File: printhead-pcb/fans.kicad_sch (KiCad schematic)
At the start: 18 parts, among them J1 FAN0, J2 FAN2, J3 FAN1, J4 FAN3, Q1 DTC143E, Q2 DTC143E, Q3 DTC143E, Q4 DTC143E, U1 EMC2302-1-AIZL-TR, U2 EMC2302-2-AIZL-TR

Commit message: layout
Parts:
- removed U1: EMC2302-1-AIZL-TR, EMC2302-1-AIZL-TR:MSOP10_MC_MCH-M, symbol EMC2302-1-AIZL-TR:EMC2302-1-AIZL-TR
- added U1: EMC2302-2-AIZL-TR, EMC2302-2-AIZL-TR:MSOP10_MC_MCH, symbol EMC2302-2-AIZL-TR:EMC2302-2-AIZL-TR
- J2: renamed from J1; footprint Connector_JST:JST_GH_SM02B-GHS-TB_1x02-1MP_P1.25mm_Horizontal -> Connector_JST:JST_EH_S2B-EH_1x02_P2.50mm_Horizontal
- J3: renamed from J2; footprint Connector_JST:JST_GH_SM02B-GHS-TB_1x02-1MP_P1.25mm_Horizontal -> Connector_JST:JST_EH_B2B-EH-A_1x02_P2.50mm_Vertical
- J4: renamed from J3; footprint Connector_JST:JST_GH_SM02B-GHS-TB_1x02-1MP_P1.25mm_Horizontal -> Connector_JST:JST_EH_S2B-EH_1x02_P2.50mm_Horizontal
- J5: renamed from J4; footprint Connector_JST:JST_GH_SM02B-GHS-TB_1x02-1MP_P1.25mm_Horizontal -> Connector_JST:JST_EH_B2B-EH-A_1x02_P2.50mm_Vertical
- R6: renamed from R5; value 3k3 -> 10k
- R7: renamed from R6; value 3k3 -> 10k
- U2: footprint EMC2302-1-AIZL-TR:MSOP10_MC_MCH-M -> EMC2302-2-AIZL-TR:MSOP10_MC_MCH
- renumbered R9 to R10, R10 to R11, R3 to R4, R4 to R5, R7 to R8, R8 to R9
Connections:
- net +3V3: now also U1.3 (VDD)
- net FAN_0_PWM: now also U1.5 (PWM1)
- net FAN_1_PWM: now also U1.7 (PWM2)
- net GND: now also U1.4 (GND)
- net SCL: now also U1.2 (SMCLK)
- net SDA: now also U1.1 (SMDATA)
- net at R6.1: now also U1.10 (*ALERT)
- net at R4.1: now also U1.6 (TACH1)
- net at R8.1: now also U1.8 (TACH2)
- net at R10.1: now also U1.9 (CLK)

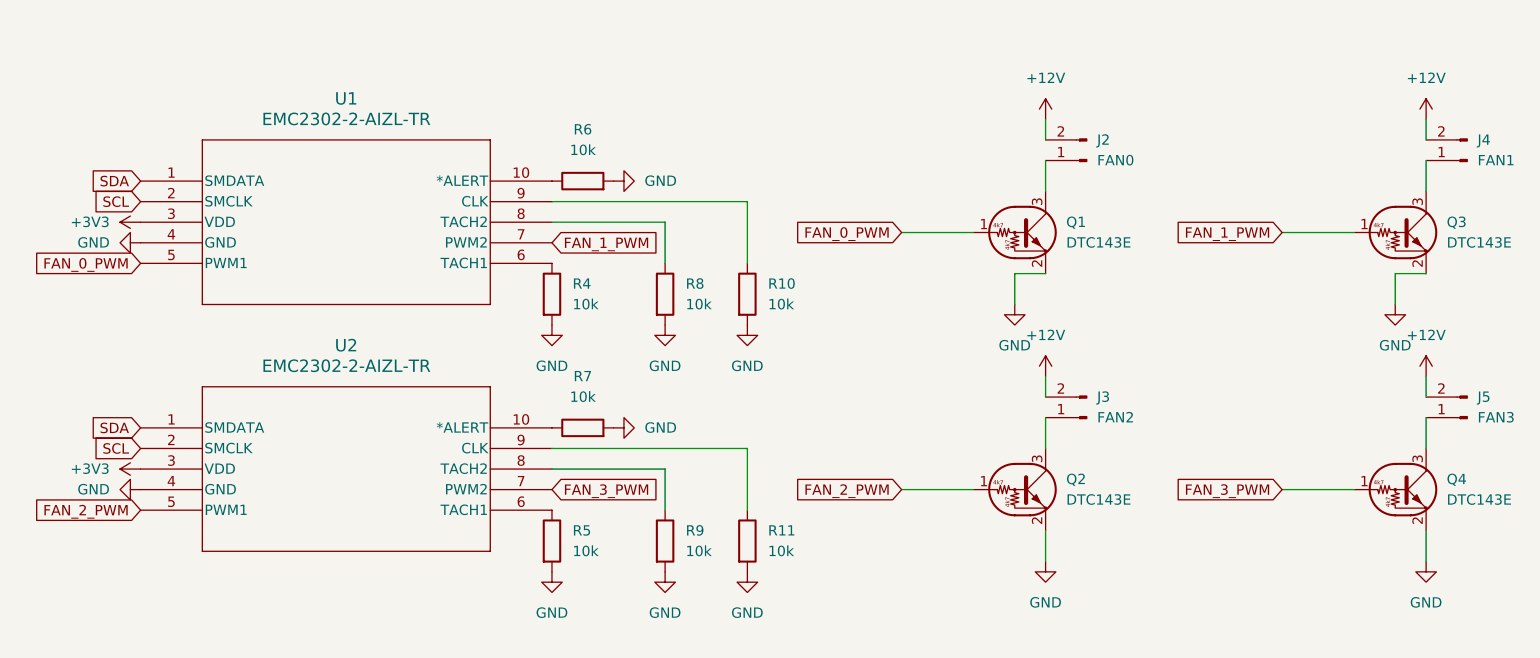
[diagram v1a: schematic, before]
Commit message: add pwr, gnd 5V for di2c chip
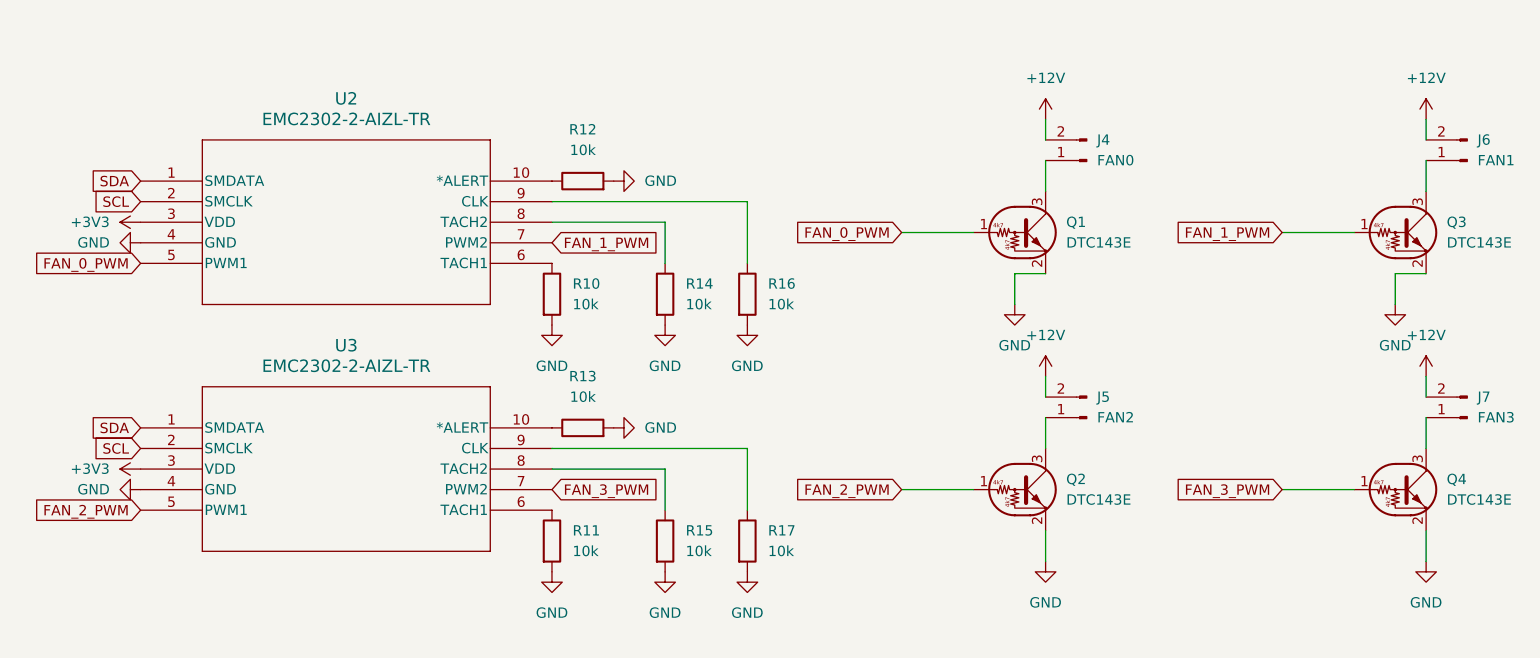
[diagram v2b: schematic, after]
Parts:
- renumbered J2 to J4, J3 to J5, J4 to J6, J5 to J7, R4 to R10, R5 to R11, R6 to R12, R7 to R13, R8 to R14, R9 to R15, R10 to R16, R11 to R17, U1 to U2, U2 to U3

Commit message: added voltage converter
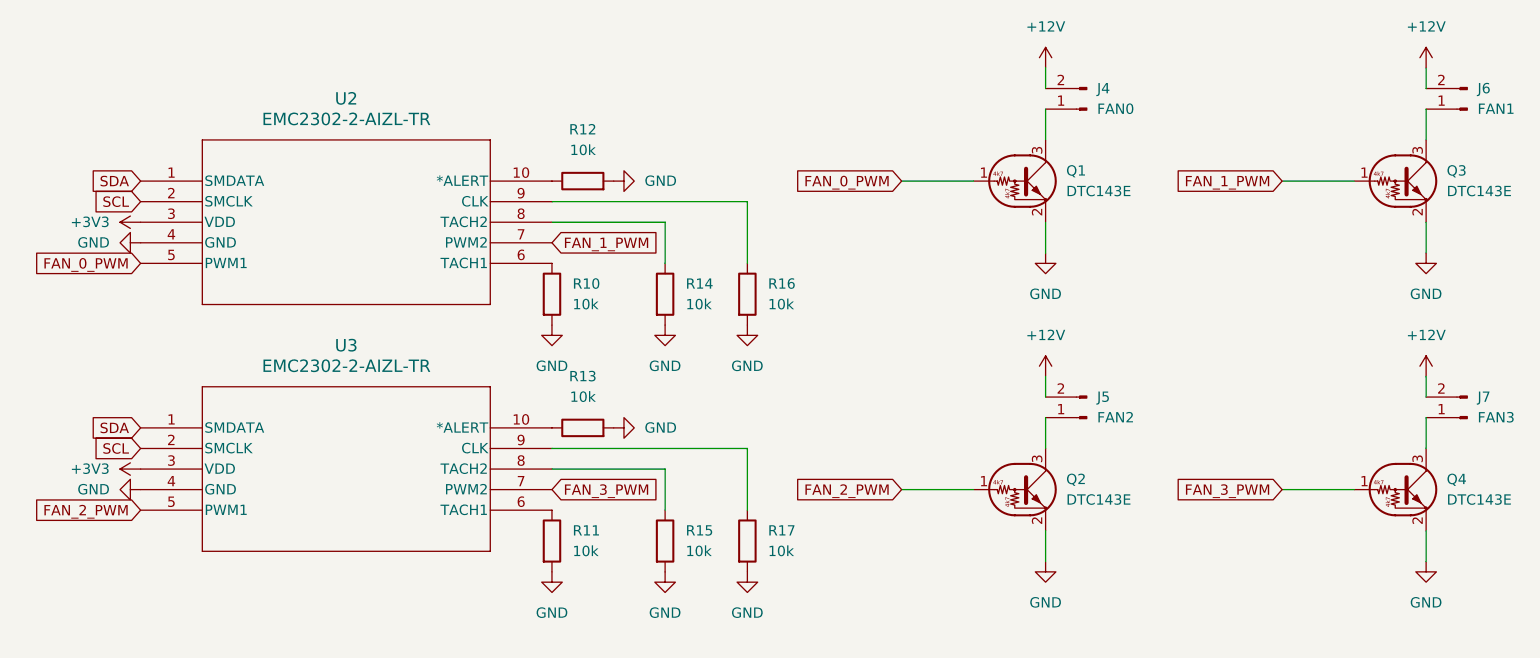
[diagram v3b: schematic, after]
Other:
- moved on the sheet: J4, J6, Q1, Q3
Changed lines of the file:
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@@
 	(wire
 		(pts
-			(xy 162.56 83.82) (xy 171.45 83.82)
+			(xy 162.56 77.47) (xy 171.45 77.47)
 		)
 		(stroke
@@
 	(wire
 		(pts
-			(xy 180.34 69.85) (xy 180.34 72.39)
+			(xy 180.34 63.5) (xy 180.34 66.04)
 		)
 		(stroke
@@
 	(wire
 		(pts
-			(xy 180.34 74.93) (xy 180.34 78.74)
+			(xy 180.34 68.58) (xy 180.34 72.39)
 		)
 		(stroke
@@
 	(wire
 		(pts
-			(xy 227.33 69.85) (xy 227.33 72.39)
+			(xy 227.33 63.5) (xy 227.33 66.04)
 		)
 		(stroke
@@
 	(wire
 		(pts
-			(xy 223.52 88.9) (xy 227.33 88.9)
+			(xy 180.34 106.68) (xy 180.34 110.49)
 		)
 		(stroke
@@
 	(wire
 		(pts
-			(xy 180.34 106.68) (xy 180.34 110.49)
+			(xy 133.35 82.55) (xy 119.38 82.55)
 		)
 		(stroke
@@
 	(wire
 		(pts
-			(xy 133.35 82.55) (xy 119.38 82.55)
+			(xy 227.33 68.58) (xy 227.33 72.39)
 		)
 		(stroke
@@
 	(wire
 		(pts
-			(xy 227.33 74.93) (xy 227.33 78.74)
+			(xy 180.34 82.55) (xy 180.34 86.36)
 		)
 		(stroke
@@
 	(wire
 		(pts
-			(xy 176.53 88.9) (xy 176.53 92.71)
+			(xy 209.55 77.47) (xy 218.44 77.47)
 		)
 		(stroke
@@
 	(wire
 		(pts
-			(xy 209.55 83.82) (xy 218.44 83.82)
+			(xy 180.34 101.6) (xy 180.34 104.14)
 		)
 		(stroke
@@
 	(wire
 		(pts
-			(xy 180.34 101.6) (xy 180.34 104.14)
+			(xy 227.33 82.55) (xy 227.33 86.36)
 		)
 		(stroke
@@
 	(wire
 		(pts
-			(xy 223.52 88.9) (xy 223.52 92.71)
+			(xy 227.33 101.6) (xy 227.33 104.14)
 		)
 		(stroke
@@
 		)
 	)
-	(wire
-		(pts
-			(xy 176.53 88.9) (xy 180.34 88.9)
-		)
-		(stroke
-			(width 0)
-			(type default)
-		)
-	)
-	(wire
-		(pts
-			(xy 227.33 101.6) (xy 227.33 104.14)
-		)
-		(stroke
-			(width 0)
-			(type default)
-		)
-	)
 	(global_label "FAN_3_PWM"
 		(shape input)
@@
 	(global_label "FAN_0_PWM"
 		(shape input)
-		(at 162.56 83.82 180)
+		(at 162.56 77.47 180)
 		(fields_autoplaced yes)
 		(effects
@@
 		)
 		(property "Intersheetrefs" "${INTERSHEET_REFS}"
-			(at 148.7496 83.82 0)
+			(at 148.7496 77.47 0)
 			(effects
 				(font
@@
 	(global_label "FAN_1_PWM"
 		(shape input)
-		(at 209.55 83.82 180)
+		(at 209.55 77.47 180)
 		(fields_autoplaced yes)
 		(effects
@@
 		)
 		(property "Intersheetrefs" "${INTERSHEET_REFS}"
-			(at 195.7396 83.82 0)
+			(at 195.7396 77.47 0)
 			(effects
 				(font
@@
 	(symbol
 		(lib_id "power:+12V")
-		(at 180.34 69.85 0)
+		(at 180.34 63.5 0)
 		(unit 1)
 		(exclude_from_sim no)
@@
 		(fields_autoplaced yes)
 		(property "Reference" "#PWR032"
-			(at 180.34 73.66 0)
+			(at 180.34 67.31 0)
 			(effects
 				(font
@@
 		)
 		(property "Value" "+12V"
-			(at 180.34 64.77 0)
+			(at 180.34 58.42 0)
 			(effects
 				(font
@@
 		)
 		(property "Footprint" ""
-			(at 180.34 69.85 0)
+			(at 180.34 63.5 0)
 			(effects
 				(font
@@
 		)
 		(property "Datasheet" ""
-			(at 180.34 69.85 0)
+			(at 180.34 63.5 0)
 			(effects
 				(font
@@
 		)
 		(property "Description" "Power symbol creates a global label with name \"+12V\""
-			(at 180.34 69.85 0)
+			(at 180.34 63.5 0)
 			(effects
 				(font
@@
 	(symbol
 		(lib_id "power:GND")
-		(at 176.53 92.71 0)
+		(at 180.34 86.36 0)
 		(unit 1)
 		(exclude_from_sim no)
@@
 		(fields_autoplaced yes)
 		(property "Reference" "#PWR031"
-			(at 176.53 99.06 0)
+			(at 180.34 92.71 0)
 			(effects
 				(font
@@
 		)
 		(property "Value" "GND"
-			(at 176.53 97.79 0)
+			(at 180.34 91.44 0)
 			(effects
 				(font
@@
 		)
 		(property "Footprint" ""
-			(at 176.53 92.71 0)
+			(at 180.34 86.36 0)
 			(effects
 				(font
@@
 		)
 		(property "Datasheet" ""
-			(at 176.53 92.71 0)
+			(at 180.34 86.36 0)
 			(effects
 				(font
@@
 		)
 		(property "Description" "Power symbol creates a global label with name \"GND\" , ground"
-			(at 176.53 92.71 0)
+			(at 180.34 86.36 0)
 			(effects
 				(font
@@
 	(symbol
 		(lib_id "Connector:Conn_01x02_Male")
-		(at 185.42 74.93 180)
+		(at 185.42 68.58 180)
 		(unit 1)
 		(exclude_from_sim no)
@@
 		(fields_autoplaced yes)
 		(property "Reference" "J4"
-			(at 186.69 72.3899 0)
+			(at 186.69 66.0399 0)
 			(effects
 				(font
@@
 		)
 		(property "Value" "FAN0"
-			(at 186.69 74.9299 0)
+			(at 186.69 68.5799 0)
 			(effects
 				(font
@@
 		)
 		(property "Footprint" "Connector_JST:JST_EH_S2B-EH_1x02_P2.50mm_Horizontal"
-			(at 185.42 74.93 0)
+			(at 185.42 68.58 0)
 			(effects
 				(font
@@
 		)
 		(property "Datasheet" "~"
-			(at 185.42 74.93 0)
+			(at 185.42 68.58 0)
 			(effects
 				(font
@@
 		)
 		(property "Description" "Generic connector, single row, 01x02, script generated (kicad-library-utils/schlib/autogen/connector/)"
-			(at 185.42 74.93 0)
+			(at 185.42 68.58 0)
 			(effects
 				(font
@@
 	(symbol
 		(lib_id "power:GND")
-		(at 223.52 92.71 0)
+		(at 227.33 86.36 0)
 		(unit 1)
 		(exclude_from_sim no)
@@
 		(fields_autoplaced yes)
 		(property "Reference" "#PWR035"
-			(at 223.52 99.06 0)
+			(at 227.33 92.71 0)
 			(effects
 				(font
@@
 		)
 		(property "Value" "GND"
-			(at 223.52 97.79 0)
+			(at 227.33 91.44 0)
 			(effects
 				(font
@@
 		)
 		(property "Footprint" ""
-			(at 223.52 92.71 0)
+			(at 227.33 86.36 0)
 			(effects
 				(font
@@
 		)
 		(property "Datasheet" ""
-			(at 223.52 92.71 0)
+			(at 227.33 86.36 0)
 			(effects
 				(font
@@
 		)
 		(property "Description" "Power symbol creates a global label with name \"GND\" , ground"
-			(at 223.52 92.71 0)
+			(at 227.33 86.36 0)
 			(effects
 				(font
@@
 	(symbol
 		(lib_id "Connector:Conn_01x02_Male")
-		(at 232.41 74.93 180)
+		(at 232.41 68.58 180)
 		(unit 1)
 		(exclude_from_sim no)
@@
 		(fields_autoplaced yes)
 		(property "Reference" "J6"
-			(at 233.68 72.3899 0)
+			(at 233.68 66.0399 0)
 			(effects
 				(font
@@
 		)
 		(property "Value" "FAN1"
-			(at 233.68 74.9299 0)
+			(at 233.68 68.5799 0)
 			(effects
 				(font
@@
 		)
 		(property "Footprint" "Connector_JST:JST_EH_S2B-EH_1x02_P2.50mm_Horizontal"
-			(at 232.41 74.93 0)
+			(at 232.41 68.58 0)
 			(effects
 				(font
@@
 		)
 		(property "Datasheet" "~"
-			(at 232.41 74.93 0)
+			(at 232.41 68.58 0)
 			(effects
 				(font
@@
 		)
 		(property "Description" "Generic connector, single row, 01x02, script generated (kicad-library-utils/schlib/autogen/connector/)"
-			(at 232.41 74.93 0)
+			(at 232.41 68.58 0)
 			(effects
 				(font
@@
 	(symbol
 		(lib_id "power:+12V")
-		(at 227.33 69.85 0)
+		(at 227.33 63.5 0)
 		(unit 1)
 		(exclude_from_sim no)
@@
 		(fields_autoplaced yes)
 		(property "Reference" "#PWR036"
-			(at 227.33 73.66 0)
+			(at 227.33 67.31 0)
 			(effects
 				(font
@@
 		)
 		(property "Value" "+12V"
-			(at 227.33 64.77 0)
+			(at 227.33 58.42 0)
 			(effects
 				(font
@@
 		)
 		(property "Footprint" ""
-			(at 227.33 69.85 0)
+			(at 227.33 63.5 0)
 			(effects
 				(font
@@
 		)
 		(property "Datasheet" ""
-			(at 227.33 69.85 0)
+			(at 227.33 63.5 0)
 			(effects
 				(font
@@
 		)
 		(property "Description" "Power symbol creates a global label with name \"+12V\""
-			(at 227.33 69.85 0)
+			(at 227.33 63.5 0)
 			(effects
 				(font
@@
 	(symbol
 		(lib_id "Transistor_BJT:DTC143E")
-		(at 224.79 83.82 0)
+		(at 224.79 77.47 0)
 		(unit 1)
 		(exclude_from_sim no)
@@
 		(fields_autoplaced yes)
 		(property "Reference" "Q3"
-			(at 229.87 82.5499 0)
+			(at 229.87 76.1999 0)
 			(effects
 				(font
@@
 		)
 		(property "Value" "DTC143E"
-			(at 229.87 85.0899 0)
+			(at 229.87 78.7399 0)
 			(effects
 				(font
@@
 		)
 		(property "Footprint" "Package_TO_SOT_SMD:SOT-723"
-			(at 224.79 83.82 0)
+			(at 224.79 77.47 0)
 			(effects
 				(font
@@
 		)
 		(property "Datasheet" ""
-			(at 224.79 83.82 0)
+			(at 224.79 77.47 0)
 			(effects
 				(font
@@
 		)
 		(property "Description" "Digital NPN Transistor, 4k7/4k7, SOT-23"
-			(at 224.79 83.82 0)
+			(at 224.79 77.47 0)
 			(effects
 				(font
@@
 	(symbol
 		(lib_id "Transistor_BJT:DTC143E")
-		(at 177.8 83.82 0)
+		(at 177.8 77.47 0)
 		(unit 1)
 		(exclude_from_sim no)
@@
 		(fields_autoplaced yes)
 		(property "Reference" "Q1"
-			(at 182.88 82.5499 0)
+			(at 182.88 76.1999 0)
 			(effects
 				(font
@@
 		)
 		(property "Value" "DTC143E"
-			(at 182.88 85.0899 0)
+			(at 182.88 78.7399 0)
 			(effects
 				(font
@@
 		)
 		(property "Footprint" "Package_TO_SOT_SMD:SOT-723"
-			(at 177.8 83.82 0)
+			(at 177.8 77.47 0)
 			(effects
 				(font
@@
 		)
 		(property "Datasheet" ""
-			(at 177.8 83.82 0)
+			(at 177.8 77.47 0)
 			(effects
 				(font
@@
 		)
 		(property "Description" "Digital NPN Transistor, 4k7/4k7, SOT-23"
-			(at 177.8 83.82 0)
-			(effects
-				(font
+			(at 177.8 77.47 0)
+			(effects
+				(font
